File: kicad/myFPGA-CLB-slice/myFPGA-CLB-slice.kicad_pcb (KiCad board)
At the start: 4 copper layers, 157 parts, among them J1 Conn_01x04, J12 Conn_01x04, J13 Conn_01x04, J14 Conn_01x04, J15 Conn_01x04, J2 Conn_01x04, J3 Conn_01x04, J4 Conn_01x04, J5 Conn_01x04, J6 Conn_01x04, J7 Conn_01x04, J8 Conn_01x02, J9 Conn_01x02, U1 NC7SB3157P6X, U10 NC7SB3157P6X, U11 NC7SB3157P6X, U12 NC7SB3157P6X, U13 74LS157, U14 NC7SB3157P6X, U15 NC7SB3157P6X, U16 NC7SB3157P6X, U17 NC7SB3157P6X, U18 74LS175, U19 74AHCT595, U2 74AHCT595, U20 74AHCT595, U21 74LS151, U22 74LS151, U23 NC7SB3157P6X, U24 74AHCT595, U25 74AHCT595, U26 74LS151, U27 74LS151, U28 NC7SB3157P6X, U29 74AHCT595, U3 74AHCT595, U30 74AHCT595, U31 74LS151, U32 74LS151, U33 NC7SB3157P6X, U34 74LS153, U35 74LS153, U36 74LS153, U37 74LS153, U38 74AHCT595, U4 74AHCT595, U5 74LS151, U6 74LS151, U7 NC7SB3157P6X, U8 74HC86, U9 NC7SB3157P6X

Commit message: kicad: picked JLC parts, fixed routing to match VHDL, started layouting
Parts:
- removed R2, R3: 100k, Resistor_SMD:R_0603_1608Metric
- R1, R20, R21, R22, R23, R24, R25, R26, R27, R29, R31, R33, R35, R37, R39, R41, R43: value 100k -> 10k
- U18: footprint Package_SO:SOIC-16W_5.3x10.2mm_P1.27mm -> Package_SO:SOIC-16_3.9x9.9mm_P1.27mm
- U21, U22, U26, U27, U31, U32, U5, U6: footprint Package_SO:SOIC-16W_5.3x10.2mm_P1.27mm -> Package_SO:TSSOP-16_4.4x5mm_P0.65mm
- U34, U35, U36, U37: footprint Package_SO:SOIC-16_3.9x9.9mm_P1.27mm -> Package_SO:TSSOP-16_4.4x5mm_P0.65mm
- U8: footprint Package_SO:SOIC-16W_5.3x10.2mm_P1.27mm -> Package_SO:TSSOP-14_4.4x5mm_P0.65mm
- moved U23 140.8 mm to (152.5, 79.3)
- moved C24 136.3 mm to (138.3, 69.6)
- moved C20 131.6 mm to (152.4, 76.7)
- moved C22 129.4 mm to (142.0, 75.5)
- moved U19 128.9 mm to (132.3, 74.0), turned to 180 degrees
- moved U21 127.9 mm to (144.0, 71.5), turned to 180 degrees
- moved C14 125.8 mm to (163.5, 132.7)
- moved R1 124.3 mm to (109.0, 128.2)
- moved C36 124.3 mm to (116.5, 53.5), turned to 180 degrees
- moved U8 124.2 mm to (163.5, 128.9)
- moved C23 123.9 mm to (142.0, 86.0)
- moved R43 123.9 mm to (110.5, 57.1)
- moved C21 121.0 mm to (137.9, 80.0)
- moved R39 120.5 mm to (110.5, 68.7)
- moved U20 115.5 mm to (132.3, 84.5), turned to 180 degrees
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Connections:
- C21 pad 1: +3V3 -> +3.3VP
- C22 pad 1: +3V3 -> +3.3VP
- C23 pad 1: +3V3 -> +3.3VP
- C24 pad 1: +3V3 -> +3.3VP
- C26 pad 1: +3V3 -> +3.3VP
- C27 pad 1: +3V3 -> +3.3VP
- C28 pad 1: +3V3 -> +3.3VP
- C29 pad 1: +3V3 -> +3.3VP
- C31 pad 1: +3V3 -> +3.3VP
- C32 pad 1: +3V3 -> +3.3VP
- C33 pad 1: +3V3 -> +3.3VP
- C34 pad 1: +3V3 -> +3.3VP
- C6 pad 1: +3V3 -> +3.3VP
- C7 pad 1: +3V3 -> +3.3VP
- C8 pad 1: +3V3 -> +3.3VP
- C9 pad 1: +3V3 -> +3.3VP
- R24 pad 1: /B0 -> unconnected-(R24-Pad1)
- U19 pad 16: +3V3 -> +3.3VP
- U20 pad 16: +3V3 -> +3.3VP
- U21 pad 16: +3V3 -> unconnected-(U21-VCC-Pad16)
- U22 pad 16: +3V3 -> +3.3VP
- U24 pad 16: +3V3 -> +3.3VP
- U25 pad 16: +3V3 -> +3.3VP
- U26 pad 16: +3V3 -> unconnected-(U26-VCC-Pad16)
- U27 pad 16: +3V3 -> +3.3VP
- U29 pad 16: +3V3 -> +3.3VP
- U3 pad 14: /LUT4_0/MOSI -> /Input Selector/MISO
- U3 pad 16: +3V3 -> +3.3VP
- U30 pad 16: +3V3 -> +3.3VP
- U31 pad 16: +3V3 -> unconnected-(U31-VCC-Pad16)
- U32 pad 16: +3V3 -> +3.3VP
- U34 pad 11: unconnected-(U34-I1b-Pad11) -> /CBpre_1
- U34 pad 5: unconnected-(U34-I1a-Pad5) -> /CBw_3
- U35 pad 11: unconnected-(U35-I1b-Pad11) -> /CBpre_1
- U35 pad 5: unconnected-(U35-I1a-Pad5) -> /CBw_2
- U36 pad 11: unconnected-(U36-I1b-Pad11) -> /CBpre_1
- U36 pad 16: +3V3 -> unconnected-(U36-VCC-Pad16)
- U36 pad 5: unconnected-(U36-I1a-Pad5) -> /CBw_1
- U36 pad 7: /B0 -> unconnected-(U36-Za-Pad7)
- U37 pad 11: unconnected-(U37-I1b-Pad11) -> /CBpre_1
- U37 pad 5: unconnected-(U37-I1a-Pad5) -> /CBw_0
- U4 pad 16: +3V3 -> +3.3VP
- U5 pad 16: +3V3 -> unconnected-(U5-VCC-Pad16)
- U6 pad 16: +3V3 -> +3.3VP
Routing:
- net GND: track 12.1 -> 179.8 mm, vias 4 -> 24
- net /Input Selector/MISO: track 0.00 -> 79.8 mm, vias 0 -> 2
- net insel_d_0: track 0.00 -> 73.2 mm, vias 0 -> 2
- net /CBpre_0: track 0.00 -> 69.6 mm, vias 0 -> 4
- net insel_d_1: track 0.00 -> 69.0 mm, vias 0 -> 2
- net /CBpre_1: track 0.00 -> 64.8 mm, vias 0 -> 4
- net insel_c_0: track 0.00 -> 62.7 mm, vias 0 -> 2
- net insel_c_1: track 0.00 -> 59.8 mm, vias 0 -> 2
- net /Input Selector/CBN_3: track 0.00 -> 58.3 mm, vias 0 -> 3
- net /Input Selector/CBN_0: track 0.00 -> 58.0 mm, vias 0 -> 2
- net insel_b_0: track 0.00 -> 53.3 mm, vias 0 -> 2
- net /Input Selector/CBN_2: track 0.00 -> 49.3 mm, vias 0 -> 2
- net insel_b_1: track 0.00 -> 49.0 mm, vias 0 -> 2
- net /Input Selector/CBN_1: track 0.00 -> 47.6 mm, vias 0 -> 2
- net +3.3VP: track 0.00 -> 46.4 mm, vias 0 -> 4
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- added copper zone on In2.Cu, net +3V3
- added copper zone on In1.Cu, net GND
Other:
- board outline added: 100 x 100 mm

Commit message: restart PCB layout
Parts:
- J1, J12, J13, J14, J15, J2, J3, J4, J5, J6, J7: footprint Connector_PinHeader_2.54mm:PinHeader_1x04_P2.54mm_Vertical -> Connector_PinHeader_2.54mm:PinHeader_1x04_P2.54mm_Horizontal
- J8, J9: footprint Connector_PinHeader_2.54mm:PinHeader_1x02_P2.54mm_Vertical -> Connector_PinHeader_2.54mm:PinHeader_1x02_P2.54mm_Horizontal
- moved J12 129.9 mm to (62.0, 34.0)
- moved J2 125.0 mm to (55.0, 54.0), turned to 180 degrees
- moved R7 121.1 mm to (119.1, 154.4), turned to 180 degrees
- moved R8 119.8 mm to (119.1, 151.4), turned to 180 degrees
- moved U2 119.6 mm to (122.5, 161.1), turned to 90 degrees
- moved R9 118.6 mm to (119.1, 148.5), turned to 180 degrees
- moved R10 117.7 mm to (119.1, 145.6), turned to 180 degrees
- moved R11 116.8 mm to (119.1, 142.6), turned to 180 degrees
- moved J6 116.4 mm to (54.0, 146.0), turned to 180 degrees
- moved J15 113.0 mm to (140.0, 46.4), turned to 0 degrees
- moved R4 111.6 mm to (123.5, 145.6), turned to 180 degrees
- moved C4 111.0 mm to (58.0, 145.0), turned to 90 degrees
- moved R5 110.7 mm to (123.5, 142.6), turned to 180 degrees
- moved R6 109.9 mm to (123.5, 139.7), turned to 180 degrees
- moved D1 109.3 mm to (127.9, 154.4), turned to 180 degrees
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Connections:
- J14 pad 1: SCLK -> GND
- J14 pad 2: MISO -> LATCH
- J14 pad 3: LACTH -> MISO
- J14 pad 4: GND -> SCLK
- J15 pad 1: GND -> /clk_1
- J15 pad 2: /clk_0 -> GND
- J15 pad 3: GND -> /clk_0
- J15 pad 4: /clk_1 -> GND
- J7 pad 1: +3V3 -> +3.3VP
- J7 pad 4: +3.3VP -> +3V3
- R24 pad 1: unconnected-(R24-Pad1) -> /B0
- U19 pad 12: REG -> LATCH
- U2 pad 12: REG -> LATCH
- U20 pad 12: REG -> LATCH
- U21 pad 16: unconnected-(U21-VCC-Pad16) -> +3.3VP
- U24 pad 12: REG -> LATCH
- U25 pad 12: REG -> LATCH
- U26 pad 16: unconnected-(U26-VCC-Pad16) -> +3.3VP
- U29 pad 12: REG -> LATCH
- U3 pad 12: REG -> LATCH
- U30 pad 12: REG -> LATCH
- U31 pad 16: unconnected-(U31-VCC-Pad16) -> +3.3VP
- U36 pad 16: unconnected-(U36-VCC-Pad16) -> +3V3
- U38 pad 12: LATCH -> /Input Selector/LATCH
- U4 pad 12: REG -> LATCH
- U5 pad 16: unconnected-(U5-VCC-Pad16) -> +3.3VP
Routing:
- net LATCH: track 1.80 -> 156.8 mm, vias 1 -> 8
- net SCLK: track 1.81 -> 155.4 mm, vias 1 -> 8
- net +3.3VP: track 46.4 -> 176.0 mm, vias 4 -> 16
- net GND: track 179.8 -> 298.8 mm, vias 24 -> 31
- net /Input Selector/MISO: track 79.8 -> 0.00 mm, vias 2 -> 0
- net /CBpre_1: track 64.8 -> 0.00 mm, vias 4 -> 0
- net insel_d_1: track 69.0 -> 16.4 mm, vias 2 -> 0
- net insel_d_0: track 73.2 -> 22.2 mm, vias 2 -> 0
- net /Input Selector/CBN_2: track 49.3 -> 0.00 mm, vias 2 -> 0
- net insel_c_1: track 59.8 -> 16.4 mm, vias 2 -> 0
- net insel_c_0: track 62.7 -> 22.2 mm, vias 2 -> 0
- net insel_b_1: track 49.0 -> 16.4 mm, vias 2 -> 0
- net /Input Selector/CBN_0: track 58.0 -> 89.3 mm
- net insel_b_0: track 53.3 -> 22.2 mm, vias 2 -> 0
- net /CBw_3: track 30.9 -> 0.00 mm, vias 1 -> 0
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- removed copper zone on In2.Cu, net +3V3
- removed copper zone on In1.Cu, net GND
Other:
- board size 100 x 100 mm -> 100 x 140 mm
- board text added: "https://www.ismolex.com/wp-content/uploads/2016/11/2.54mm-right-angle-female-header.png"
- board text added: "https://www.ismolex.com/wp-content/uploads/2016/11/2.54mm-right-angle-single-row-pin-header-1.png"

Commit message: progress in pcb of CLB
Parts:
- moved R1 128.2 mm to (160.2, 50.0)
- moved U1 128.2 mm to (160.3, 46.9)
- moved C25 10.6 mm to (109.0, 92.5), turned to 180 degrees
- moved C20 9.75 mm to (109.0, 67.5), turned to 180 degrees
- moved C5 9.38 mm to (109.0, 42.5), turned to 180 degrees
- moved C30 9.36 mm to (109.0, 117.5), turned to 180 degrees
- moved U13 7.61 mm to (128.0, 69.8)
- moved U28 5.81 mm to (109.0, 95.0), turned to 0 degrees
- moved C13 5.59 mm to (109.0, 128.5), turned to 180 degrees
- moved U9 5.54 mm to (109.0, 126.0), turned to 0 degrees
- moved R12 5.43 mm to (112.0, 126.0)
- moved U23 4.95 mm to (109.0, 70.0), turned to 0 degrees
- moved R15 4.93 mm to (112.0, 51.0)
- moved U33 4.74 mm to (109.0, 120.0), turned to 0 degrees
- moved U7 4.58 mm to (109.0, 45.0), turned to 0 degrees
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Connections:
- U18 pad 1: +3V3 -> aresetn
- U36 pad 7: unconnected-(U36-Za-Pad7) -> /B0
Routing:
- net GND: track 298.8 -> 1251.9 mm, vias 31 -> 54
- net +3V3: track 44.2 -> 284.7 mm, vias 8 -> 18
- net +3.3VP: track 176.0 -> 380.0 mm
- net /cin: track 0.00 -> 161.5 mm, vias 0 -> 3
- net /CBpre_2: track 0.00 -> 122.0 mm, vias 0 -> 8
- net /Carry Chain/carry_a: track 0.00 -> 112.4 mm, vias 0 -> 3
- net /Input Selector/CBS_0: track 0.00 -> 104.8 mm, vias 0 -> 2
- net /Input Selector/CBS_3: track 0.00 -> 104.6 mm, vias 0 -> 3
- net /CBpre_3: track 0.00 -> 104.3 mm, vias 0 -> 4
- net /clk_0: track 21.2 -> 121.9 mm
- net /clk_1: track 26.8 -> 122.4 mm
- net /CBpre_1: track 0.00 -> 91.0 mm, vias 0 -> 4
- net /La: track 0.00 -> 89.8 mm
- net /Input Selector/CBS_1: track 0.00 -> 87.5 mm, vias 0 -> 2
- net /Input Selector/CBS_2: track 0.00 -> 85.2 mm, vias 0 -> 2
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
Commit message: progress in pcb of CLB
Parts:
- removed D1, D2: LED (green), LED_SMD:LED_0805_2012Metric
- removed R4, R5: 330R, Resistor_SMD:R_0603_1608Metric
- added C40: 100n, Capacitor_SMD:C_0603_1608Metric, F.Cu at (122.5, 64.0)
- added C41: 100n, Capacitor_SMD:C_0603_1608Metric, F.Cu at (125.0, 127.0)
- added C42: 100n, Capacitor_SMD:C_0603_1608Metric, F.Cu at (127.0, 81.3)
- moved R10 55.8 mm to (170.2, 123.3)
- moved R11 55.8 mm to (170.2, 120.3)
- moved R6 55.8 mm to (174.6, 117.4)
- moved R7 55.8 mm to (170.2, 132.1)
- moved R9 55.8 mm to (170.2, 126.2)
- moved D3 55.8 mm to (179.0, 126.0)
- moved D4 55.8 mm to (179.0, 123.0)
- moved D6 55.8 mm to (179.0, 116.9)
- moved D7 55.8 mm to (179.0, 113.8)
- moved D5 55.8 mm to (179.0, 119.9)
- moved D8 55.8 mm to (179.0, 110.8)
- moved R8 55.8 mm to (170.2, 129.2)
- moved U1 46.3 mm to (127.0, 79.0)
- moved R1 40.3 mm to (131.2, 78.0)
- moved U2 40.2 mm to (125.0, 121.0), turned to 180 degrees
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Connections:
- U2 pad 6: Net-(U2-QG) -> unconnected-(U2-QG-Pad6)
- U2 pad 7: Net-(U2-QH) -> unconnected-(U2-QH-Pad7)
- U38 pad 12: /Input Selector/LATCH -> LATCH
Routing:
- net GND: track 1251.9 -> 1712.8 mm, vias 54 -> 63
- net SCLK: track 148.8 -> 342.5 mm, vias 9 -> 14
- net +3V3: track 284.7 -> 471.4 mm, vias 18 -> 25
- net LATCH: track 150.5 -> 327.8 mm, vias 9 -> 11
- net +3.3VP: track 380.0 -> 491.2 mm, vias 16 -> 20
- net /Input Selector/MISO: track 0.00 -> 107.7 mm, vias 0 -> 2
- net MOSI: track 0.00 -> 98.9 mm, vias 0 -> 1
- net MISO: track 0.00 -> 73.8 mm, vias 0 -> 1
- net insel_d_1: track 16.7 -> 86.5 mm, vias 0 -> 4
- net insel_d_0: track 22.3 -> 89.4 mm, vias 0 -> 4
- net insel_c_1: track 18.7 -> 75.9 mm, vias 0 -> 4
- net insel_c_0: track 22.4 -> 76.3 mm, vias 0 -> 4
- net insel_b_1: track 18.4 -> 62.7 mm, vias 0 -> 4
- net insel_b_0: track 22.5 -> 64.4 mm, vias 0 -> 4
- net insel_a_1: track 18.2 -> 55.7 mm, vias 0 -> 2
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
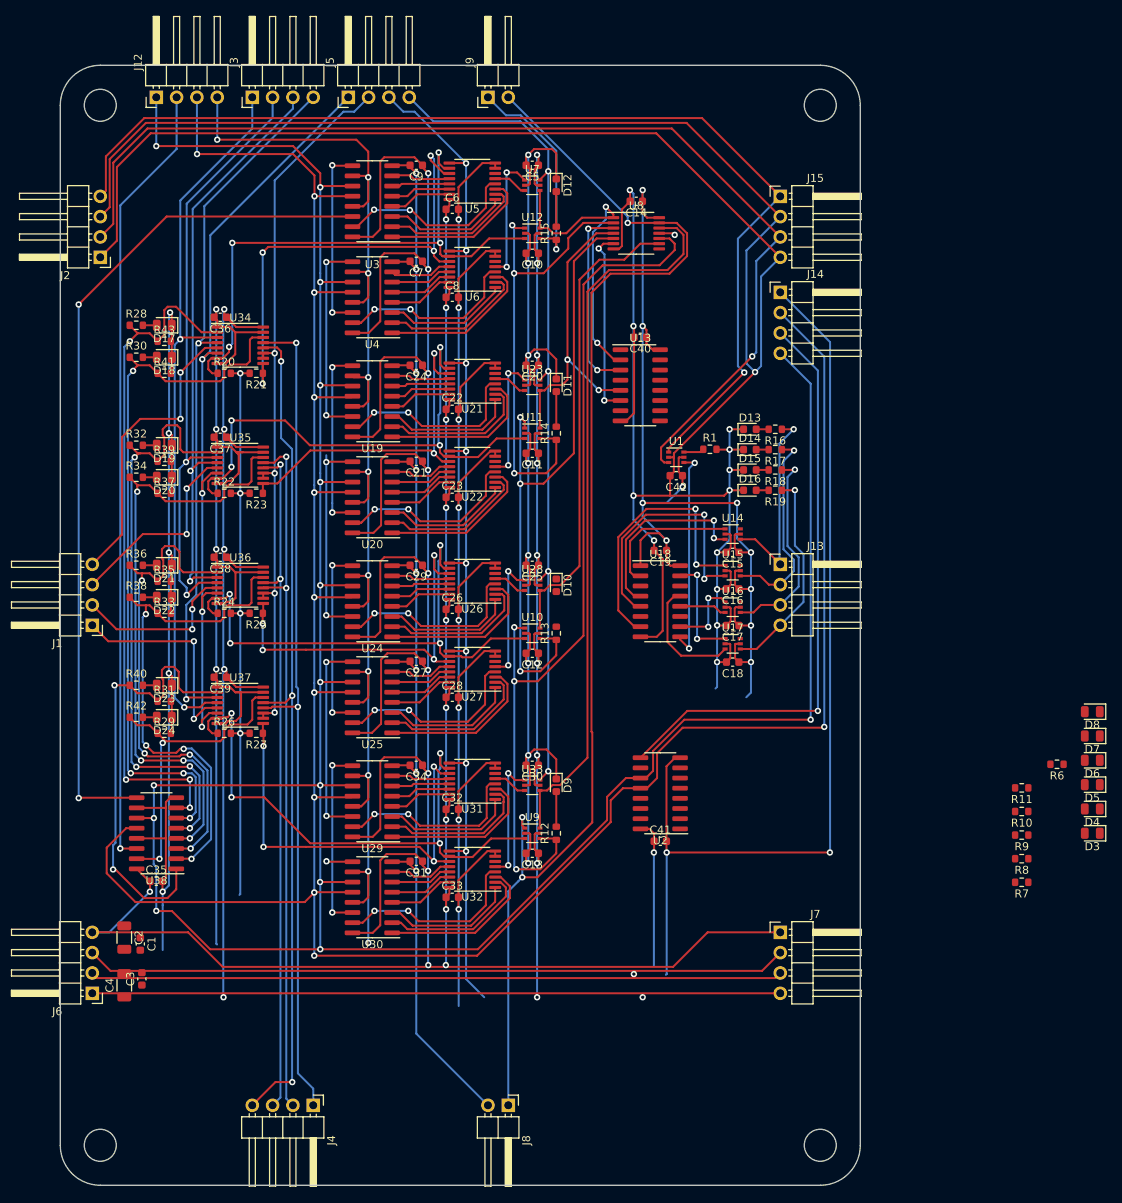
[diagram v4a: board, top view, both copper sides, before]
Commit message: 2 layer pcb for clb seems complete (awaits review)
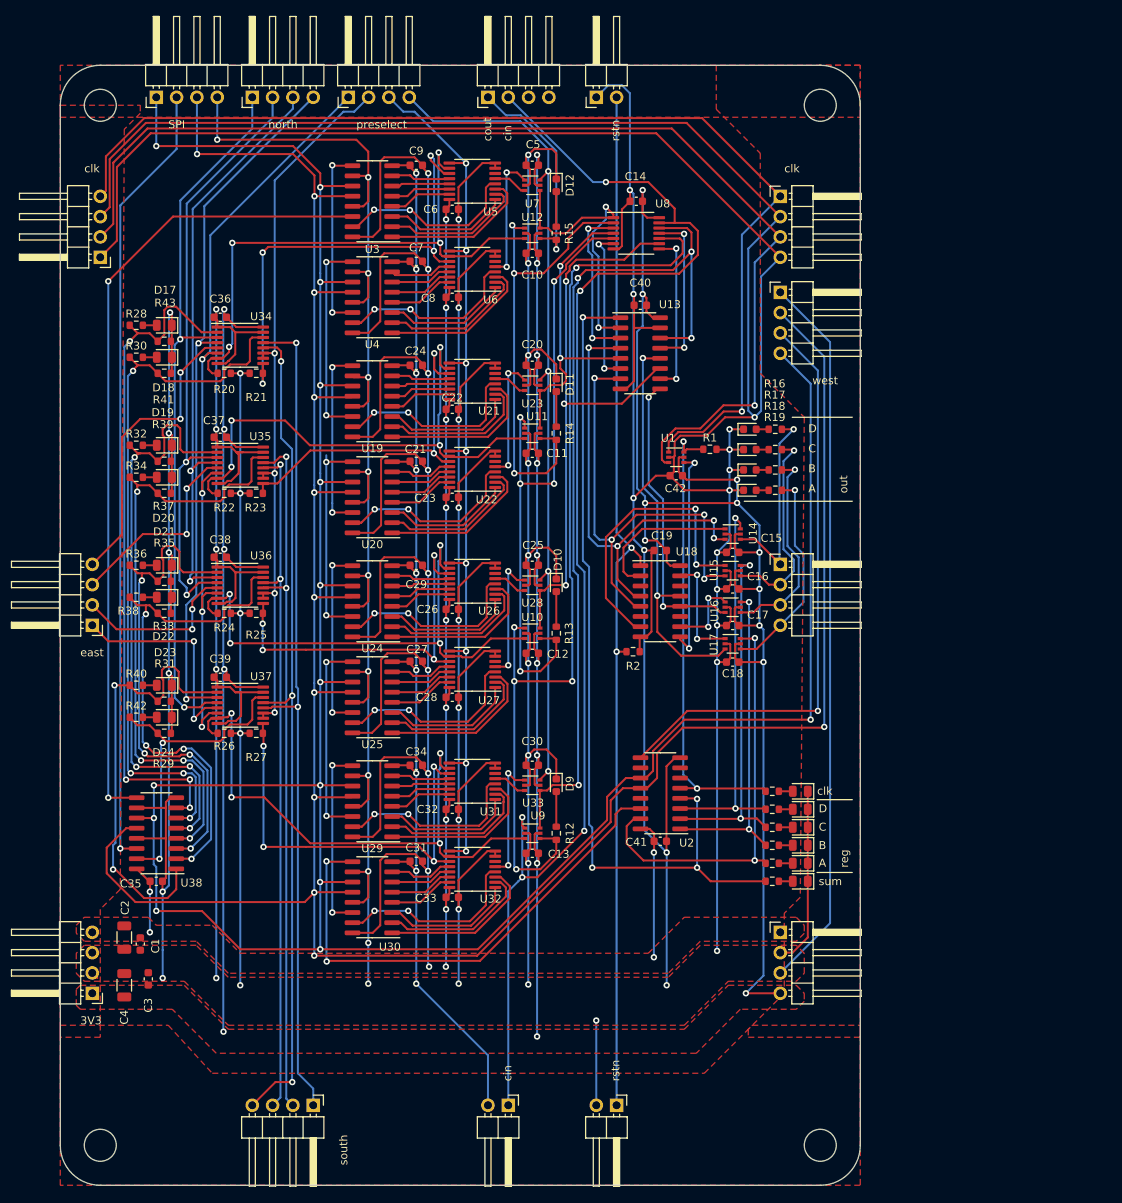
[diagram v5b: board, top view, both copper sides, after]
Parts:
- added J10: Conn_01x02, Connector_PinHeader_2.54mm:PinHeader_1x02_P2.54mm_Horizontal, F.Cu at (119.5, 160.0)
- added J11: Conn_01x02, Connector_PinHeader_2.54mm:PinHeader_1x02_P2.54mm_Horizontal, F.Cu at (117.0, 34.0)
- added R2: 10k, Resistor_SMD:R_0603_1608Metric, F.Cu at (121.6, 103.3)
- J9: value Conn_01x02 -> Conn_01x04; footprint Connector_PinHeader_2.54mm:PinHeader_1x02_P2.54mm_Horizontal -> Connector_PinHeader_2.54mm:PinHeader_1x04_P2.54mm_Horizontal
- moved D8 41.1 mm to (142.5, 129.8)
- moved D7 39.0 mm to (142.5, 127.5)
- moved D4 37.6 mm to (142.5, 132.0)
- moved D6 37.4 mm to (142.5, 125.2)
- moved D3 36.9 mm to (142.5, 120.8)
- moved D5 36.6 mm to (142.5, 123.0)
- moved R6 35.7 mm to (139.0, 120.8), turned to 0 degrees
- moved R11 32.6 mm to (139.0, 129.8), turned to 0 degrees
- moved R8 31.8 mm to (139.0, 123.0), turned to 0 degrees
- moved R10 31.5 mm to (139.0, 127.5), turned to 0 degrees
- moved R9 31.2 mm to (139.0, 125.2), turned to 0 degrees
- moved R7 31.2 mm to (139.0, 132.0), turned to 0 degrees
- moved C40 4.00 mm to (122.5, 60.0)
- moved U13 4.00 mm to (122.5, 66.0)
- moved C3 0.80 mm to (61.0, 144.2)
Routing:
- net aresetn: track 0.00 -> 131.5 mm, vias 0 -> 2
- net set_sum: track 0.00 -> 107.1 mm, vias 0 -> 4
- net +3.3VP: track 491.2 -> 396.8 mm, vias 20 -> 22
- net /LUT4_3/MISO: track 3.27 -> 63.8 mm, vias 1 -> 2
- net set_clk_sel: track 2.57 -> 58.9 mm, vias 0 -> 2
- net set_reg_a: track 0.00 -> 52.4 mm, vias 0 -> 2
- net set_reg_d: track 0.00 -> 48.7 mm, vias 0 -> 2
- net set_reg_c: track 0.00 -> 45.0 mm, vias 0 -> 2
- net set_reg_b: track 0.00 -> 41.1 mm, vias 0 -> 2
- net /Oa: track 15.1 -> 50.8 mm, vias 0 -> 2
- net +3V3: track 471.4 -> 438.6 mm
- net /Od: track 23.9 -> 56.7 mm, vias 2 -> 4
- net /Ob: track 5.94 -> 36.8 mm, vias 0 -> 2
- net /Oc: track 32.2 -> 59.1 mm, vias 2 -> 4
- net Net-(U13-I1c): track 0.00 -> 20.5 mm, vias 0 -> 2
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- added copper zone on F.Cu, net +3.3VP
- added copper zone on F.Cu, net +3V3
- added copper zone on F.Cu, net GND
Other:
- board text added: "3V3"
- board text added: "A"
- board text added: "B"
- board text added: "C"
- board text added: "D"
- board text added: "SPI"
- board text added: "cin"
- board text added: "clk"
- board text added: "cout"
- board text added: "east"
- board text added: "north"
- board text added: "out"
- board text added: "preselect"
- board text added: "reg"
- board text added: "rstn"
- board text added: "south"
- board text added: "sum"
- board text added: "west"

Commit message: fixed a footprint
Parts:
- U34, U35, U36, U37: footprint Package_SO:TSSOP-16_4.4x5mm_P0.65mm -> Package_SO:SOIC-16_3.9x9.9mm_P1.27mm
- moved C36 2.50 mm to (70.0, 59.0)
- moved C37 2.50 mm to (70.0, 74.0)
- moved C38 2.50 mm to (70.0, 89.0)
- moved C39 2.50 mm to (70.0, 104.0)
- moved R20 2.50 mm to (70.5, 71.0)
- moved R21 2.50 mm to (74.5, 71.0)
- moved R22 2.50 mm to (70.5, 86.0)
- moved R23 2.50 mm to (74.5, 86.0)
- moved R24 2.50 mm to (70.5, 101.0)
- moved R25 2.50 mm to (74.5, 101.0)
- moved R26 2.50 mm to (70.5, 116.0)
- moved R27 2.50 mm to (74.5, 116.0)
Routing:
- net GND: track 1715.9 -> 1741.5 mm, vias 71 -> 72
- net /C0: track 68.0 -> 73.8 mm
- net insel_b_0: track 64.4 -> 68.6 mm
- net /CBpre_0: track 99.3 -> 95.3 mm
- net /CBpre_1: track 91.0 -> 94.8 mm
- net insel_a_0: track 40.1 -> 43.8 mm
- net /D0: track 72.6 -> 76.2 mm
- net +3V3: track 438.6 -> 441.7 mm
- net insel_c_0: track 76.3 -> 79.5 mm
- net insel_d_0: track 89.4 -> 92.4 mm
- net /D1: track 59.4 -> 62.2 mm
- net /B1: track 46.7 -> 44.1 mm
- net /A1: track 53.6 -> 51.6 mm
- net insel_c_1: track 75.9 -> 74.1 mm
- net /C1: track 43.4 -> 45.2 mm
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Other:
- copper layers 4 -> 2
- board text added: "CLB rev. 1"
- board text added: "bottom"
- board text added: "my 4bit FPGA"
- board text added: "top"

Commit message: fixed a footprint, changed to 2 Layer stackup
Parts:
- U34, U35, U36, U37: footprint Package_SO:SOIC-16_3.9x9.9mm_P1.27mm -> Package_SO:TSSOP-16_4.4x5mm_P0.65mm
- U8: footprint Package_SO:TSSOP-14_4.4x5mm_P0.65mm -> Package_SO:SOIC-14_3.9x8.7mm_P1.27mm
- moved C36 2.50 mm to (70.0, 61.5)
- moved C37 2.50 mm to (70.0, 76.5)
- moved C38 2.50 mm to (70.0, 91.5)
- moved C39 2.50 mm to (70.0, 106.5)
- moved R20 2.50 mm to (70.5, 68.5)
- moved R21 2.50 mm to (74.5, 68.5)
- moved R22 2.50 mm to (70.5, 83.5)
- moved R23 2.50 mm to (74.5, 83.5)
- moved R24 2.50 mm to (70.5, 98.5)
- moved R25 2.50 mm to (74.5, 98.5)
- moved R26 2.50 mm to (70.5, 113.5)
- moved R27 2.50 mm to (74.5, 113.5)
- moved C14 1.50 mm to (122.0, 45.5)
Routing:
- net GND: track 1741.5 -> 1725.7 mm, vias 72 -> 71
- net /C0: track 73.8 -> 68.0 mm
- net /cin: track 169.6 -> 175.2 mm
- net insel_b_0: track 68.6 -> 64.4 mm
- net /CBpre_0: track 95.3 -> 99.3 mm
- net /CBpre_1: track 94.8 -> 91.0 mm
- net insel_a_0: track 43.8 -> 40.1 mm
- net /D0: track 76.2 -> 72.6 mm
- net insel_c_0: track 79.5 -> 76.3 mm
- net insel_d_0: track 92.4 -> 89.4 mm
- net /D1: track 62.2 -> 59.4 mm
- net /B1: track 44.1 -> 46.7 mm
- net +3V3: track 441.7 -> 439.4 mm
- net /A1: track 51.6 -> 53.6 mm
- net insel_c_1: track 74.1 -> 75.9 mm
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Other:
- board text removed: "CLB rev. 1"
- board text removed: "bottom"
- board text removed: "my 4bit FPGA"
- board text removed: "top"

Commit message: gitignore fix
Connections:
- U19 pad 10: GND -> +3.3VP
- U2 pad 10: GND -> +3.3VP
- U20 pad 10: GND -> +3.3VP
- U24 pad 10: GND -> +3.3VP
- U25 pad 10: GND -> +3.3VP
- U29 pad 10: GND -> +3.3VP
- U3 pad 10: GND -> +3.3VP
- U30 pad 10: GND -> +3.3VP
- U38 pad 10: GND -> +3.3VP
- U4 pad 10: GND -> +3.3VP
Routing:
- net +3.3VP: track 396.8 -> 452.8 mm, vias 22 -> 24
- net GND: track 1725.7 -> 1676.4 mm
- net MOSI: track 98.9 -> 100.4 mm
- net LATCH: track 327.8 -> 329.1 mm
- net insel_a_1: track 55.7 -> 56.3 mm
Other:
- board text added: "BOTTOM"
- board text added: "TOP"
